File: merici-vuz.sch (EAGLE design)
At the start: 43 parts, among them IC1 MEGA328-PB, IC2 MCP73831, IC3 LE33, Q1 3,6864 MHz, T1 IRF7306

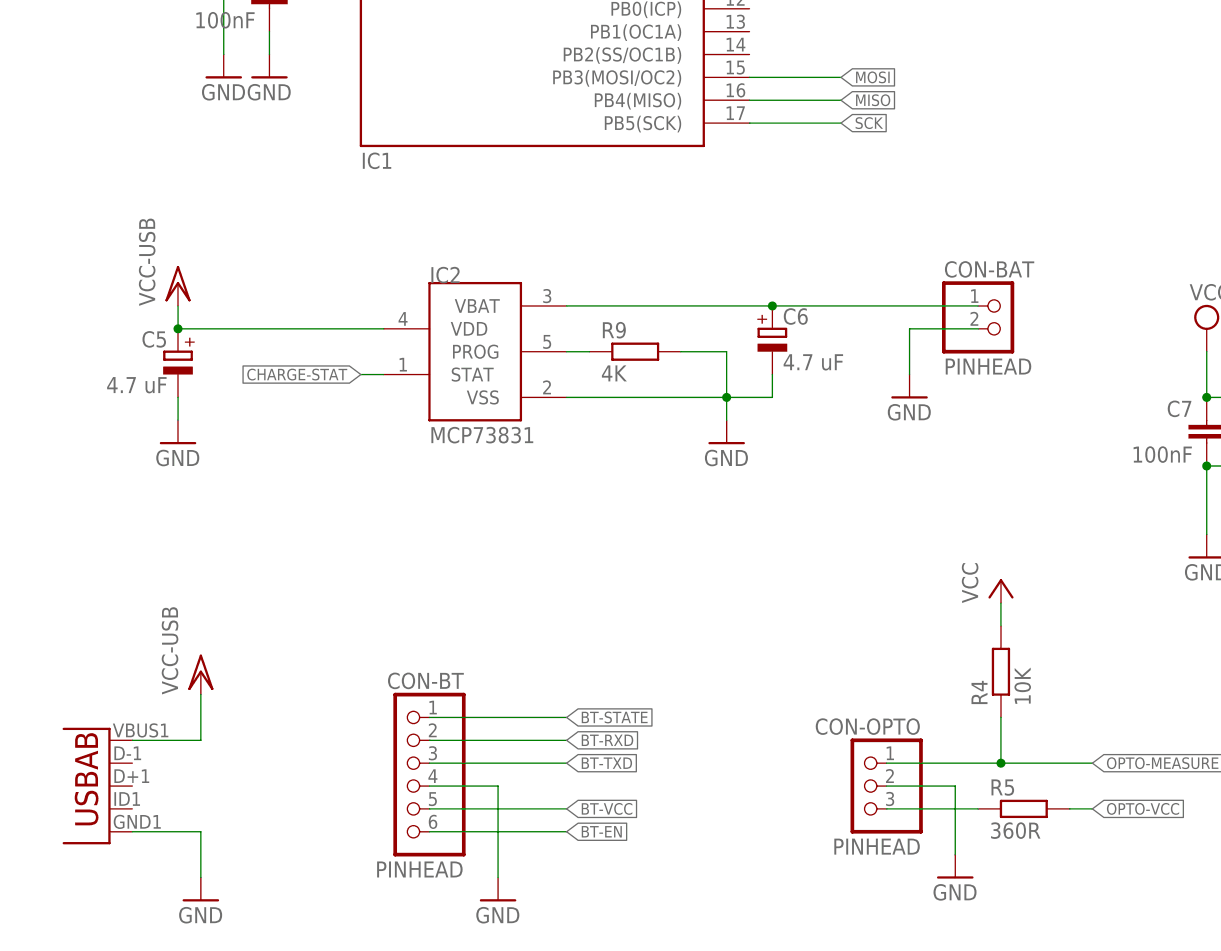
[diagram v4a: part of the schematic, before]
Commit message: Add power jumper.
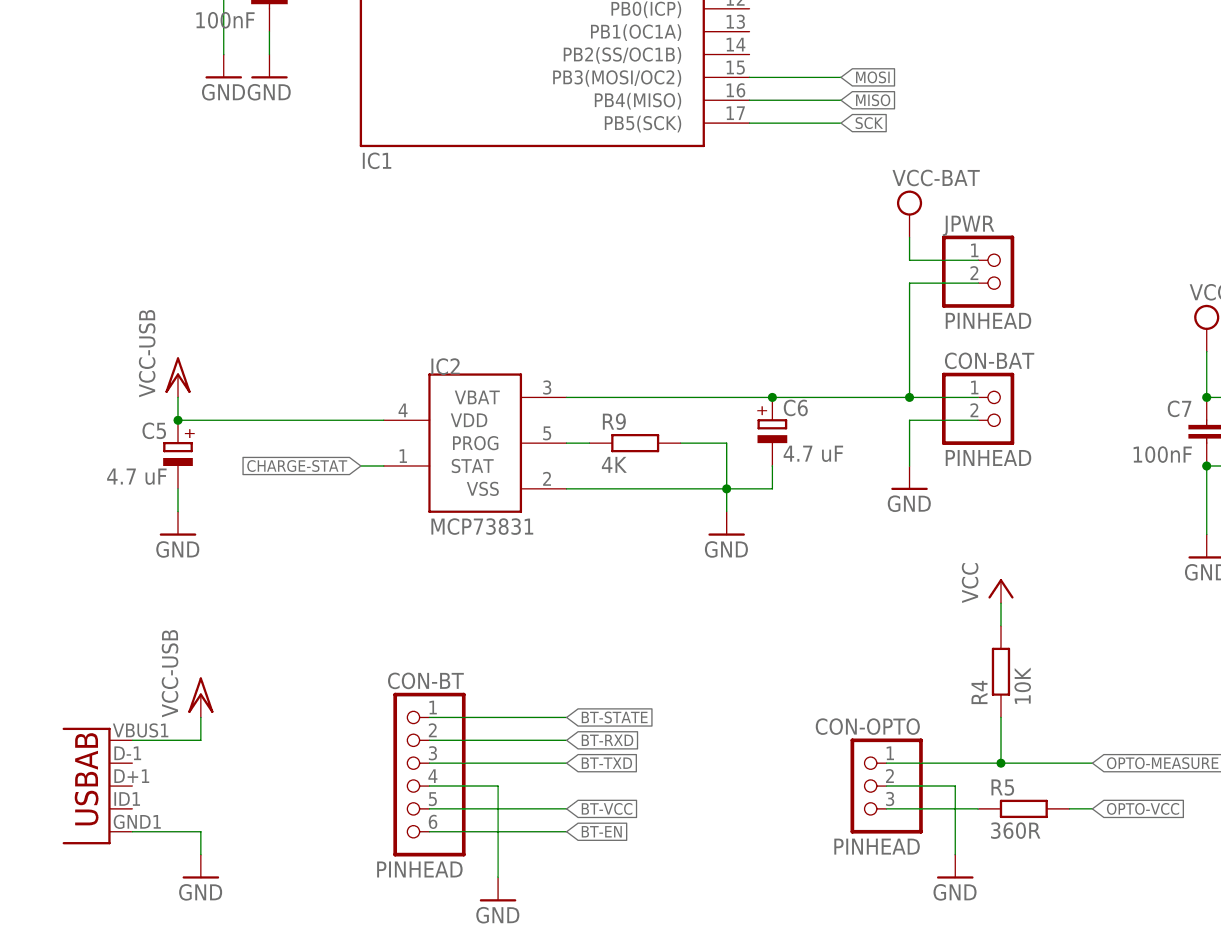
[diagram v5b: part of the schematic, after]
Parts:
- added JPWR: PINHEAD, pinhead:PINHD-1X2
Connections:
- net N$7: now also JPWR.2
- net VCC-BAT: now also JPWR.1
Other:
- moved on the sheet: C5, C6, CON-BAT, IC2, R9
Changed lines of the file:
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@@
 <part name="R12" library="rcl" deviceset="R-EU_" device="R0805" value="220R"/>
 <part name="R13" library="rcl" deviceset="R-EU_" device="R0805" value="220R"/>
+<part name="JPWR" library="pinhead" deviceset="PINHD-1X2" device="" value="PINHEAD"/>
+<part name="SUPPLY4" library="supply2" deviceset="VCC" device="" value="VCC-BAT"/>
 </parts>
 <sheets>
@@
 <instance part="R3" gate="G$1" x="243.84" y="139.7" rot="R90"/>
 <instance part="U1" gate="G$1" x="17.78" y="25.4" rot="R180"/>
-<instance part="GND3" gate="1" x="30.48" y="12.7"/>
-<instance part="P+5" gate="G$1" x="30.48" y="38.1"/>
+<instance part="GND3" gate="1" x="30.48" y="15.24"/>
+<instance part="P+5" gate="G$1" x="30.48" y="35.56"/>
 <instance part="CON-BT" gate="A" x="53.34" y="25.4" rot="MR0"/>
 <instance part="GND4" gate="1" x="63.5" y="12.7"/>
@@
 <instance part="C4" gate="G$1" x="33.02" y="147.32"/>
 <instance part="GND8" gate="1" x="33.02" y="104.14"/>
-<instance part="IC2" gate="G$1" x="60.96" y="73.66"/>
-<instance part="GND9" gate="1" x="88.9" y="63.5"/>
-<instance part="R9" gate="G$1" x="78.74" y="73.66"/>
-<instance part="P+9" gate="G$1" x="27.94" y="81.28"/>
-<instance part="C5" gate="A" x="27.94" y="73.66" rot="MR0"/>
-<instance part="GND10" gate="1" x="27.94" y="63.5"/>
-<instance part="C6" gate="A" x="93.98" y="76.2"/>
-<instance part="CON-BAT" gate="G$1" x="119.38" y="76.2"/>
-<instance part="GND11" gate="1" x="109.22" y="68.58"/>
+<instance part="IC2" gate="G$1" x="60.96" y="63.5"/>
+<instance part="GND9" gate="1" x="88.9" y="53.34"/>
+<instance part="R9" gate="G$1" x="78.74" y="63.5"/>
+<instance part="P+9" gate="G$1" x="27.94" y="71.12"/>
+<instance part="C5" gate="A" x="27.94" y="63.5" rot="MR0"/>
+<instance part="GND10" gate="1" x="27.94" y="53.34"/>
+<instance part="C6" gate="A" x="93.98" y="66.04"/>
+<instance part="CON-BAT" gate="G$1" x="119.38" y="66.04"/>
+<instance part="GND11" gate="1" x="109.22" y="58.42"/>
 <instance part="TP1" gate="G$1" x="228.6" y="40.64" rot="MR180"/>
 <instance part="TP2" gate="G$1" x="228.6" y="55.88"/>
@@
 <instance part="R12" gate="G$1" x="175.26" y="99.06"/>
 <instance part="R13" gate="G$1" x="226.06" y="99.06"/>
+<instance part="JPWR" gate="G$1" x="119.38" y="81.28"/>
+<instance part="SUPPLY4" gate="G$1" x="109.22" y="88.9"/>
 </instances>
 <busses>
@@
 <pinref part="GND3" gate="1" pin="GND"/>
 <wire x1="22.86" y1="20.32" x2="30.48" y2="20.32" width="0.1524" layer="91"/>
-<wire x1="30.48" y1="20.32" x2="30.48" y2="15.24" width="0.1524" layer="91"/>
+<wire x1="30.48" y1="20.32" x2="30.48" y2="17.78" width="0.1524" layer="91"/>
 </segment>
 <segment>
@@
 <pinref part="IC2" gate="G$1" pin="VSS"/>
 <pinref part="GND9" gate="1" pin="GND"/>
-<wire x1="71.12" y1="68.58" x2="88.9" y2="68.58" width="0.1524" layer="91"/>
-<wire x1="88.9" y1="68.58" x2="88.9" y2="66.04" width="0.1524" layer="91"/>
+<wire x1="71.12" y1="58.42" x2="88.9" y2="58.42" width="0.1524" layer="91"/>
+<wire x1="88.9" y1="58.42" x2="88.9" y2="55.88" width="0.1524" layer="91"/>
 <pinref part="R9" gate="G$1" pin="2"/>
-<wire x1="83.82" y1="73.66" x2="88.9" y2="73.66" width="0.1524" layer="91"/>
-<wire x1="88.9" y1="73.66" x2="88.9" y2="68.58" width="0.1524" layer="91"/>
-<junction x="88.9" y="68.58"/>
+<wire x1="83.82" y1="63.5" x2="88.9" y2="63.5" width="0.1524" layer="91"/>
+<wire x1="88.9" y1="63.5" x2="88.9" y2="58.42" width="0.1524" layer="91"/>
+<junction x="88.9" y="58.42"/>
 <pinref part="C6" gate="A" pin="-"/>
-<wire x1="88.9" y1="68.58" x2="93.98" y2="68.58" width="0.1524" layer="91"/>
-<wire x1="93.98" y1="68.58" x2="93.98" y2="71.12" width="0.1524" layer="91"/>
+<wire x1="88.9" y1="58.42" x2="93.98" y2="58.42" width="0.1524" layer="91"/>
+<wire x1="93.98" y1="58.42" x2="93.98" y2="60.96" width="0.1524" layer="91"/>
 </segment>
 <segment>
 <pinref part="GND10" gate="1" pin="GND"/>
 <pinref part="C5" gate="A" pin="-"/>
-<wire x1="27.94" y1="66.04" x2="27.94" y2="68.58" width="0.1524" layer="91"/>
+<wire x1="27.94" y1="55.88" x2="27.94" y2="58.42" width="0.1524" layer="91"/>
 </segment>
 <segment>
 <pinref part="CON-BAT" gate="G$1" pin="2"/>
-<wire x1="109.22" y1="76.2" x2="116.84" y2="76.2" width="0.1524" layer="91"/>
-<wire x1="109.22" y1="71.12" x2="109.22" y2="76.2" width="0.1524" layer="91"/>
+<wire x1="109.22" y1="66.04" x2="116.84" y2="66.04" width="0.1524" layer="91"/>
+<wire x1="109.22" y1="60.96" x2="109.22" y2="66.04" width="0.1524" layer="91"/>
 <pinref part="GND11" gate="1" pin="GND"/>
 </segment>
@@
 <wire x1="22.86" y1="30.48" x2="30.48" y2="30.48" width="0.1524" layer="91"/>
 <pinref part="P+5" gate="G$1" pin="VCC/2"/>
-<wire x1="30.48" y1="30.48" x2="30.48" y2="35.56" width="0.1524" layer="91"/>
+<wire x1="30.48" y1="30.48" x2="30.48" y2="33.02" width="0.1524" layer="91"/>
 </segment>
 </net>
@@
 <junction x="142.24" y="68.58"/>
 </segment>
+<segment>
+<pinref part="JPWR" gate="G$1" pin="1"/>
+<wire x1="116.84" y1="83.82" x2="109.22" y2="83.82" width="0.1524" layer="91"/>
+<pinref part="SUPPLY4" gate="G$1" pin="VCC"/>
+<wire x1="109.22" y1="83.82" x2="109.22" y2="86.36" width="0.1524" layer="91"/>
+</segment>
 </net>
 <net name="BAT-SENSE" class="0">
@@
 <pinref part="R9" gate="G$1" pin="1"/>
 <pinref part="IC2" gate="G$1" pin="PROG"/>
-<wire x1="73.66" y1="73.66" x2="71.12" y2="73.66" width="0.1524" layer="91"/>
+<wire x1="73.66" y1="63.5" x2="71.12" y2="63.5" width="0.1524" layer="91"/>
 </segment>
 </net>
@@
 <segment>
 <pinref part="IC2" gate="G$1" pin="STAT"/>
-<wire x1="50.8" y1="71.12" x2="48.26" y2="71.12" width="0.1524" layer="91"/>
-<label x="48.26" y="71.12" size="1.27" layer="95" rot="R180" xref="yes"/>
+<wire x1="50.8" y1="60.96" x2="48.26" y2="60.96" width="0.1524" layer="91"/>
+<label x="48.26" y="60.96" size="1.27" layer="95" rot="R180" xref="yes"/>
 </segment>
 <segment>
@@
 <segment>
 <pinref part="IC2" gate="G$1" pin="VDD"/>
-<wire x1="50.8" y1="76.2" x2="27.94" y2="76.2" width="0.1524" layer="91"/>
+<wire x1="50.8" y1="66.04" x2="27.94" y2="66.04" width="0.1524" layer="91"/>
 <pinref part="P+9" gate="G$1" pin="VCC/2"/>
-<wire x1="27.94" y1="76.2" x2="27.94" y2="78.74" width="0.1524" layer="91"/>
+<wire x1="27.94" y1="66.04" x2="27.94" y2="68.58" width="0.1524" layer="91"/>
 <pinref part="C5" gate="A" pin="+"/>
-<junction x="27.94" y="76.2"/>
+<junction x="27.94" y="66.04"/>
 </segment>
 <segment>
@@
 <pinref part="IC2" gate="G$1" pin="VBAT"/>
 <pinref part="C6" gate="A" pin="+"/>
-<wire x1="71.12" y1="78.74" x2="93.98" y2="78.74" width="0.1524" layer="91"/>
-<wire x1="93.98" y1="78.74" x2="116.84" y2="78.74" width="0.1524" layer="91"/>
-<junction x="93.98" y="78.74"/>
+<wire x1="71.12" y1="68.58" x2="93.98" y2="68.58" width="0.1524" layer="91"/>
+<wire x1="93.98" y1="68.58" x2="109.22" y2="68.58" width="0.1524" layer="91"/>
+<junction x="93.98" y="68.58"/>
 <pinref part="CON-BAT" gate="G$1" pin="1"/>
-</segment>
-</net>
+<pinref part="JPWR" gate="G$1" pin="2"/>
+<wire x1="109.22" y1="68.58" x2="116.84" y2="68.58" width="0.1524" layer="91"/>
+<wire x1="116.84" y1="81.28" x2="109.22" y2="81.28" width="0.1524" layer="91"/>
+<wire x1="109.22" y1="81.28" x2="109.22" y2="68.58" width="0.1524" layer="91"/>
+<junction x="109.22" y="68.58"/>
+</segment>
+</net>

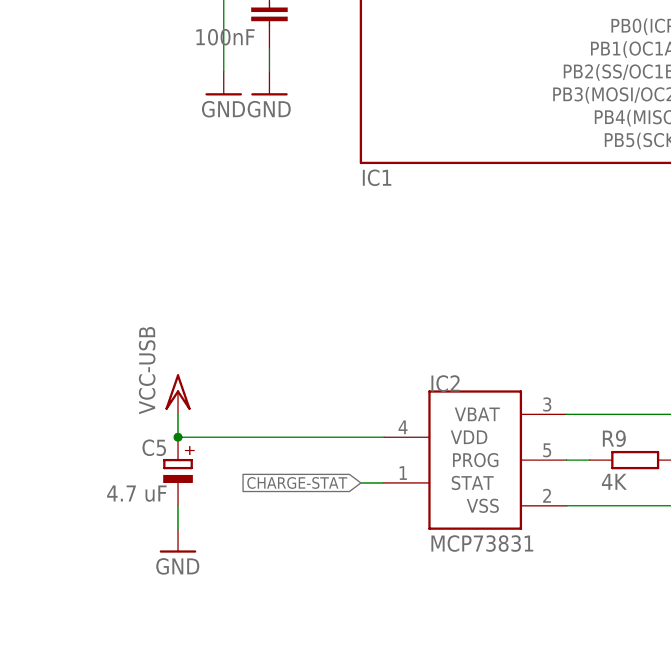
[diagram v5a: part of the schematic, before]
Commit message: Add LED to charging circuit.
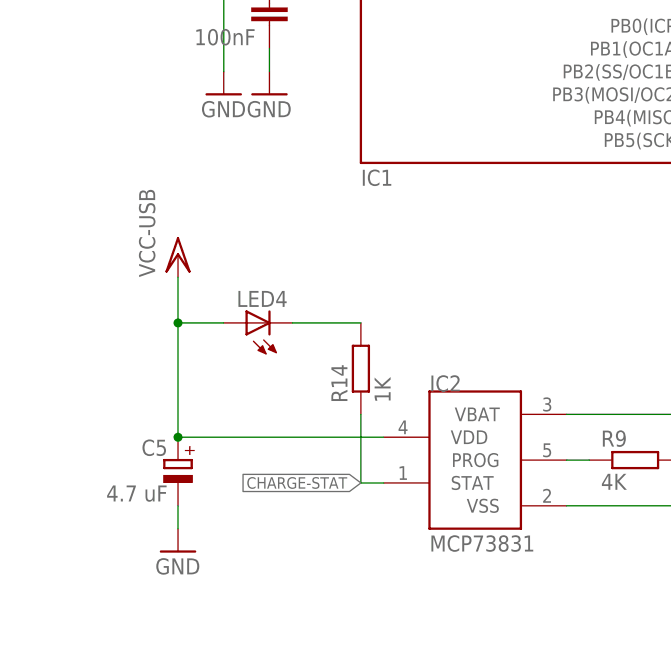
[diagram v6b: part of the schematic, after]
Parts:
- added LED4: (no value), led:LEDCHIP-LED0805
- added R14: 1K, rcl:R-EU_R0805
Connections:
- new net N$6: LED4.C, R14.2
- net CHARGE-STAT: now also R14.1
- net VCC/2: now also LED4.A
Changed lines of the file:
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@@
 <part name="JPWR" library="pinhead" deviceset="PINHD-1X2" device="" value="PINHEAD"/>
 <part name="SUPPLY4" library="supply2" deviceset="VCC" device="" value="VCC-BAT"/>
+<part name="LED4" library="led" deviceset="LED" device="CHIP-LED0805"/>
+<part name="R14" library="rcl" deviceset="R-EU_" device="R0805" value="1K"/>
 </parts>
 <sheets>
@@
 <instance part="GND9" gate="1" x="88.9" y="53.34"/>
 <instance part="R9" gate="G$1" x="78.74" y="63.5"/>
-<instance part="P+9" gate="G$1" x="27.94" y="71.12"/>
+<instance part="P+9" gate="G$1" x="27.94" y="86.36"/>
 <instance part="C5" gate="A" x="27.94" y="63.5" rot="MR0"/>
 <instance part="GND10" gate="1" x="27.94" y="53.34"/>
@@
 <instance part="JPWR" gate="G$1" x="119.38" y="81.28"/>
 <instance part="SUPPLY4" gate="G$1" x="109.22" y="88.9"/>
+<instance part="LED4" gate="G$1" x="35.56" y="78.74" rot="R90"/>
+<instance part="R14" gate="G$1" x="48.26" y="73.66" rot="R90"/>
 </instances>
 <busses>
@@
 <wire x1="50.8" y1="60.96" x2="48.26" y2="60.96" width="0.1524" layer="91"/>
 <label x="48.26" y="60.96" size="1.27" layer="95" rot="R180" xref="yes"/>
+<pinref part="R14" gate="G$1" pin="1"/>
+<wire x1="48.26" y1="60.96" x2="48.26" y2="68.58" width="0.1524" layer="91"/>
 </segment>
 <segment>
@@
 <wire x1="50.8" y1="66.04" x2="27.94" y2="66.04" width="0.1524" layer="91"/>
 <pinref part="P+9" gate="G$1" pin="VCC/2"/>
-<wire x1="27.94" y1="66.04" x2="27.94" y2="68.58" width="0.1524" layer="91"/>
+<wire x1="27.94" y1="66.04" x2="27.94" y2="78.74" width="0.1524" layer="91"/>
 <pinref part="C5" gate="A" pin="+"/>
 <junction x="27.94" y="66.04"/>
+<pinref part="LED4" gate="G$1" pin="A"/>
+<wire x1="27.94" y1="78.74" x2="27.94" y2="83.82" width="0.1524" layer="91"/>
+<wire x1="33.02" y1="78.74" x2="27.94" y2="78.74" width="0.1524" layer="91"/>
+<junction x="27.94" y="78.74"/>
 </segment>
 <segment>
@@
 </segment>
 </net>
+<net name="N$6" class="0">
+<segment>
+<pinref part="R14" gate="G$1" pin="2"/>
+<pinref part="LED4" gate="G$1" pin="C"/>
+<wire x1="48.26" y1="78.74" x2="40.64" y2="78.74" width="0.1524" layer="91"/>
+</segment>
+</net>
